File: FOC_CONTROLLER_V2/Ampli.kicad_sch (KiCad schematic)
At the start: 6 parts

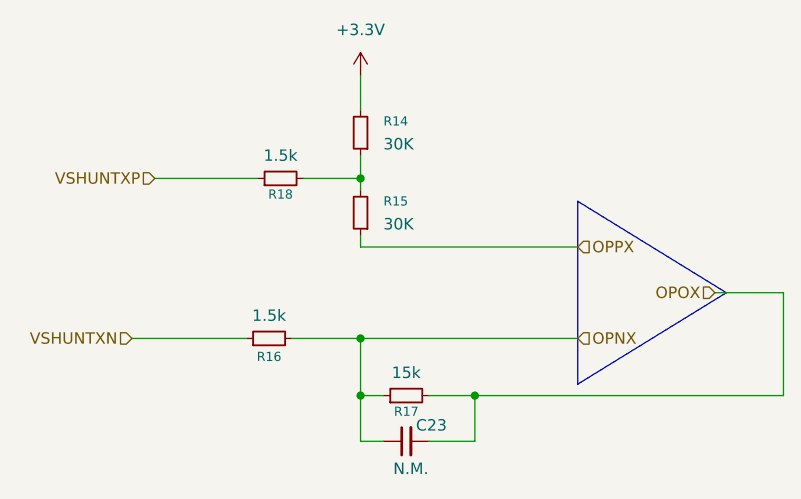
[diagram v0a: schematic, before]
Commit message: Routage Phases PCB
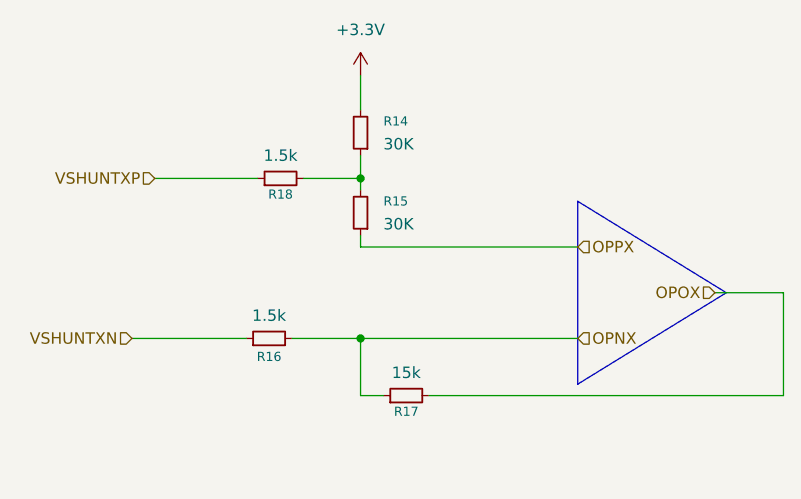
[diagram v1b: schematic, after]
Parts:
- removed C23: N.M., Capacitor_SMD:C_0603_1608Metric, symbol Device:C_Small
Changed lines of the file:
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@@
 		(color 0 0 0 0)
 	)
-	(junction
-		(at 133.35 114.3)
-		(diameter 0)
-		(color 0 0 0 0)
-	)
-	(junction
-		(at 146.05 114.3)
-		(diameter 0)
-		(color 0 0 0 0)
-	)
-	(wire
-		(pts
-			(xy 146.05 114.3) (xy 180.34 114.3)
+	(wire
+		(pts
+			(xy 140.97 114.3) (xy 180.34 114.3)
 		)
 		(stroke
@@
 	(wire
 		(pts
-			(xy 133.35 114.3) (xy 133.35 119.38)
-		)
-		(stroke
-			(width 0)
-			(type default)
-		)
-	)
-	(wire
-		(pts
-			(xy 146.05 114.3) (xy 146.05 119.38)
-		)
-		(stroke
-			(width 0)
-			(type default)
-		)
-	)
-	(wire
-		(pts
 			(xy 133.35 78.74) (xy 133.35 82.55)
 		)
@@
 	(wire
 		(pts
-			(xy 133.35 119.38) (xy 135.89 119.38)
-		)
-		(stroke
-			(width 0)
-			(type default)
-		)
-	)
-	(wire
-		(pts
 			(xy 133.35 87.63) (xy 133.35 90.17)
 		)
@@
 	(wire
 		(pts
-			(xy 146.05 119.38) (xy 140.97 119.38)
-		)
-		(stroke
-			(width 0)
-			(type default)
-		)
-	)
-	(wire
-		(pts
 			(xy 133.35 107.95) (xy 133.35 114.3)
 		)
@@
 		(pts
 			(xy 133.35 96.52) (xy 133.35 97.79)
-		)
-		(stroke
-			(width 0)
-			(type default)
-		)
-	)
-	(wire
-		(pts
-			(xy 140.97 114.3) (xy 146.05 114.3)
 		)
 		(stroke
@@
 					(unit 1)
 				)
-			)
-		)
-	)
-	(symbol
-		(lib_id "Device:C_Small")
-		(at 138.43 119.38 90)
-		(unit 1)
-		(exclude_from_sim no)
-		(in_bom yes)
-		(on_board yes)
-		(dnp no)
-		(property "Reference" "C23"
-			(at 141.224 117.602 90)
-			(effects
-				(font
-					(size 1.27 1.27)
-				)
-			)
-		)
-		(property "Value" "N.M."
-			(at 138.938 122.428 90)
-			(effects
-				(font
-					(size 1.27 1.27)
-				)
-			)
-		)
-		(property "Footprint" "Capacitor_SMD:C_0603_1608Metric"
-			(at 138.43 119.38 0)
-			(effects
-				(font
-					(size 1.27 1.27)
-				)
-				(hide yes)
-			)
-		)
-		(property "Datasheet" "~"
-			(at 138.43 119.38 0)
-			(effects
-				(font
-					(size 1.27 1.27)
-				)
-				(hide yes)
-			)
-		)
-		(property "Description" "Unpolarized capacitor, small symbol"
-			(at 138.43 119.38 0)
-			(effects
-				(font
-					(size 1.27 1.27)
-				)
-				(hide yes)
-			)
-		)
-		(pin "1"
-		)
-		(pin "2"
-		)
-		(instances
-			(project "FOC_CONTROLLER_V2"
-				(path "/a5bd1c77-2ac7-4621-b0cb-d4fae8c0736d/cbd5cfe4-ce1b-4508-8db7-1f0bf273c628"
-					(reference "C23")
-					(unit 1)
-				)
-				(path "/a5bd1c77-2ac7-4621-b0cb-d4fae8c0736d/d6028d11-a65b-4019-9e03-4484b69bb8c0"
-					(reference "C13")
-					(unit 1)
-				)
-				(path "/a5bd1c77-2ac7-4621-b0cb-d4fae8c0736d/de18a44d-679e-4741-9d64-dca0e0bbb3ff"
-					(reference "C16")
-					(unit 1)
-				)
